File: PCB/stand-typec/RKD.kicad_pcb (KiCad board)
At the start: 2 copper layers, 100 x 50 mm, 114 parts, among them J10 Conn_01x04_Male, J11 Conn_02x06_Odd_Even, J12 Conn_01x06, J13 Conn_01x03, J14 Conn_01x04, J15 Conn_01x04, J2 Conn_02x02_Odd_Even, J3 Conn_02x04_Odd_Even, J4 Conn_02x02_Odd_Even, J5 Conn_02x04_Odd_Even, K1 Key, K2 Key, K3 Key, K4 Key, P1 USB_C_Plug_USB2.0, SW2 SW_DIP_x04, SW3 SW_Push, SW5 SW_Push, U1 W25Q32JV, U2 RP2040, U3 CH9329, U4 AP1117-33, Y1 Crystal 12MHZ HC49, Y2 Crystal_GND24 12MHZ 3225

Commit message: fix pcb
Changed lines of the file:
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@@
     )
     (pad_to_mask_clearance 0)
-    (aux_axis_origin 87 130.025126)
+    (aux_axis_origin 87 87)
     (grid_origin 137 62)
     (pcbplotparams
@@
     )
   )
-  (gr_line (start 158.5 87) (end 150 87) (layer "B.SilkS") (width 0.15))
-  (gr_line (start 183.5 87) (end 158.5 87) (layer "B.SilkS") (width 0.15))
-  (gr_line (start 90.5 87) (end 150 87) (layer "B.SilkS") (width 0.15))
   (gr_line (start 170.434 50.3428) (end 173.0756 46.5836) (layer "F.SilkS") (width 0.15))
-  (gr_line (start 90.5 87) (end 150 87) (layer "F.SilkS") (width 0.15))
   (gr_line (start 100.6856 43.942) (end 103.3272 47.7266) (layer "F.SilkS") (width 0.15))
-  (gr_line (start 183.5 87) (end 158.5 87) (layer "F.SilkS") (width 0.15))
-  (gr_line (start 158.5 87) (end 150 87) (layer "F.SilkS") (width 0.15))
   (gr_line (start 103.3018 50.1142) (end 100.6602 46.609) (layer "F.SilkS") (width 0.15))
   (gr_line (start 103.3526 45.339) (end 100.6856 41.4782) (layer "F.SilkS") (width 0.15))
@@
   (gr_arc (start 187 83.5) (mid 185.974874 85.974874) (end 183.5 87) (layer "Edge.Cuts") (width 0.1))
   (gr_line (start 187 83.5) (end 187 40.5) (layer "Edge.Cuts") (width 0.1))
+  (gr_line (start 183.5 87) (end 90.5 87) (layer "Edge.Cuts") (width 0.1))
   (gr_arc (start 183.5 37) (mid 185.974874 38.025126) (end 187 40.5) (layer "Edge.Cuts") (width 0.1))
   (gr_line (start 87 40.5) (end 87 83.5) (layer "Edge.Cuts") (width 0.1))

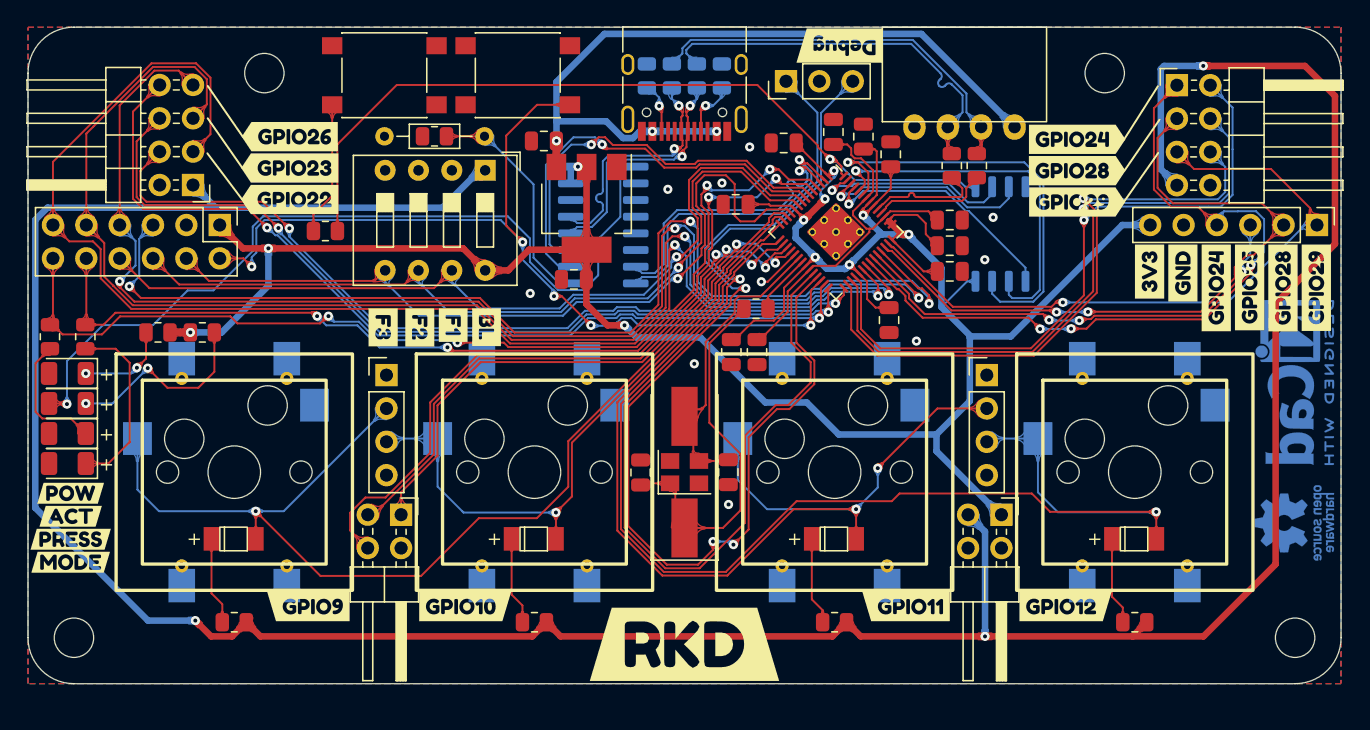
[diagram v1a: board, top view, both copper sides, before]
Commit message: 修复typec版本的接口只能在特定一面使用
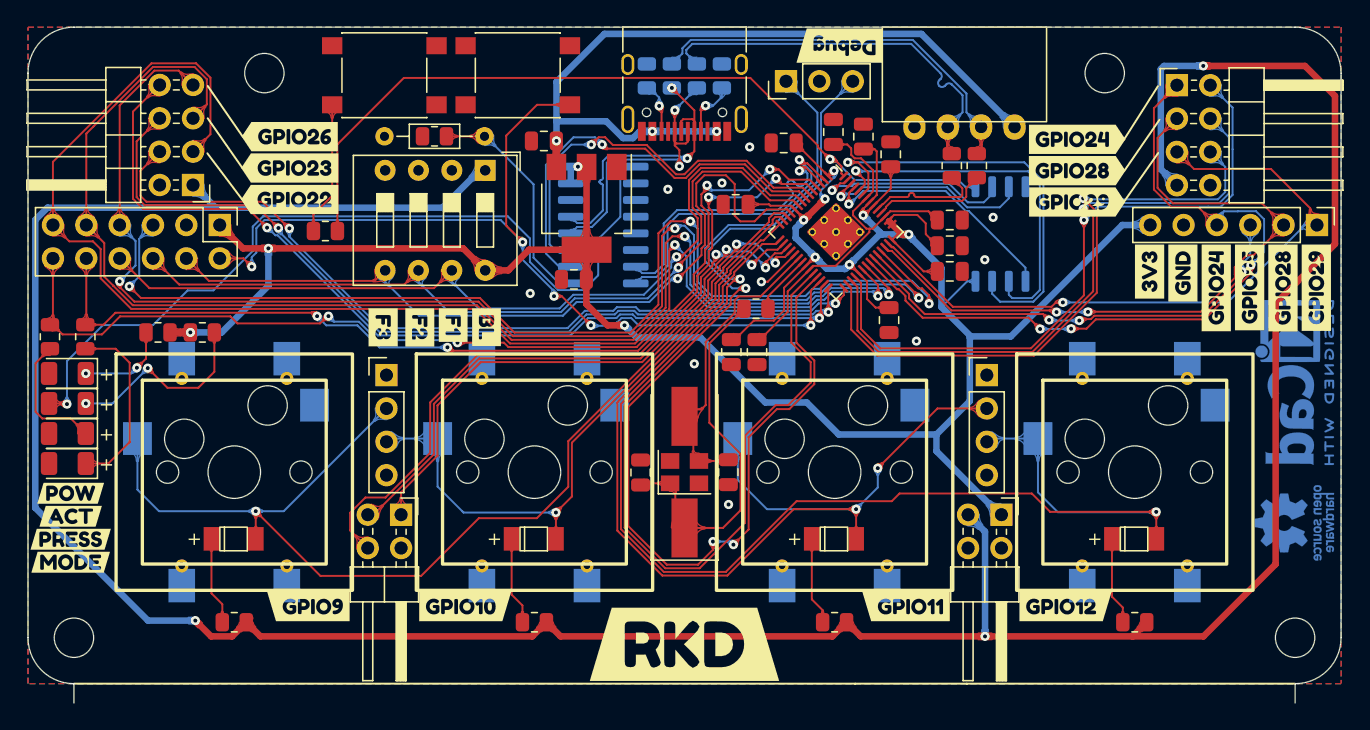
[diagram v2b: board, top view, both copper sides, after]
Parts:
- J1: renamed from P1; value USB_C_Plug_USB2.0 -> USB_C_Receptacle_USB2.0
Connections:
- J1 pad A8: (no net) -> unconnected-(J1-PadA8)
- J1 pad B6: (no net) -> /D+
- J1 pad B7: (no net) -> /D-
- J1 pad B8: (no net) -> unconnected-(J1-PadB8)
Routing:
- net /D+: track 18.9 -> 22.7 mm
- net /D-: track 18.9 -> 22.7 mm
- net /SET: track 30.5 -> 31.1 mm
- net /DEF: track 31.9 -> 32.5 mm
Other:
- board size 100 x 50 mm -> 100 x 51.5 mm
